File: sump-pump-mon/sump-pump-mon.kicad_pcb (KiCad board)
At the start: 2 copper layers, 111.8 x 61 mm, 37 parts, among them J1 Main Input, J2 Wall Power, J3 Battery, J4 Display_Conn, J5 Aux Input, J6 I2C, SW3 MODE, SW4 POWER, U1 L7805, U2 4N25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

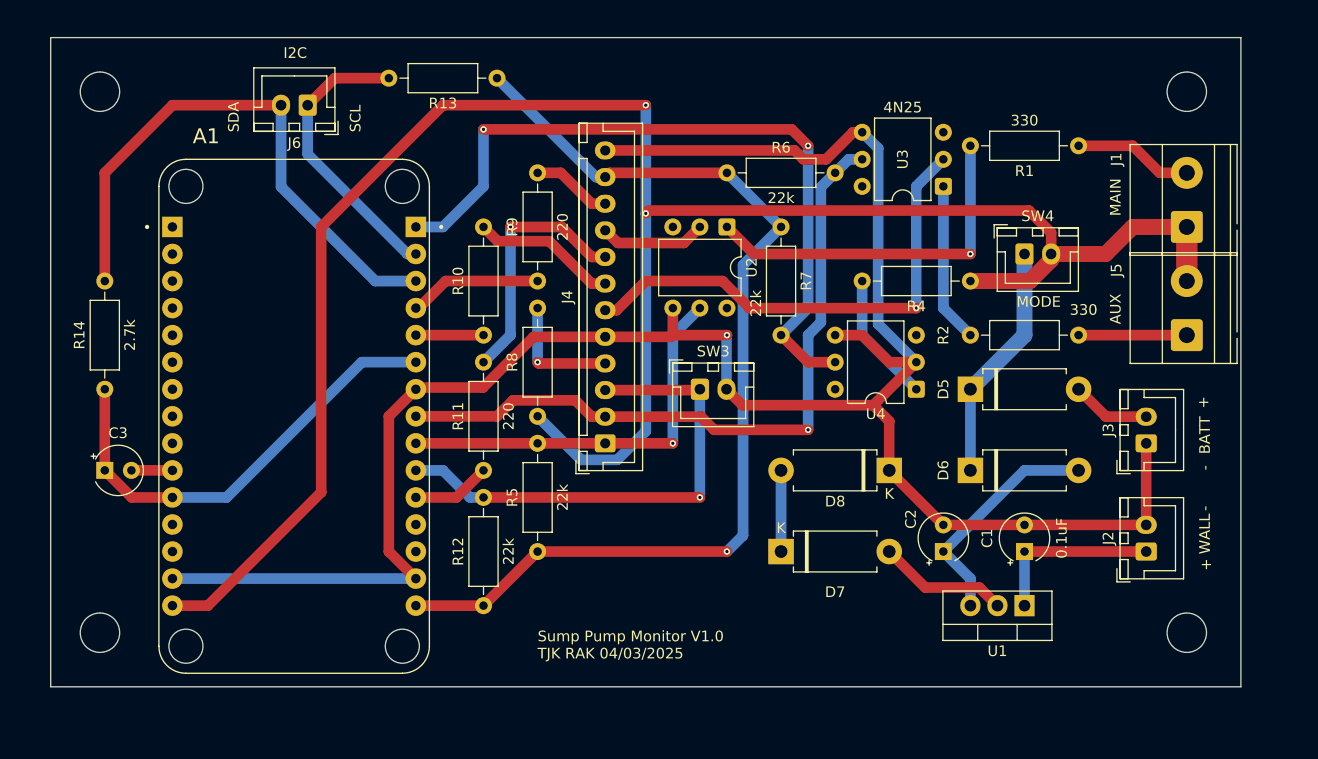
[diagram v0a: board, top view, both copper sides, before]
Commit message: Redid layout to shrink size and add ground plane
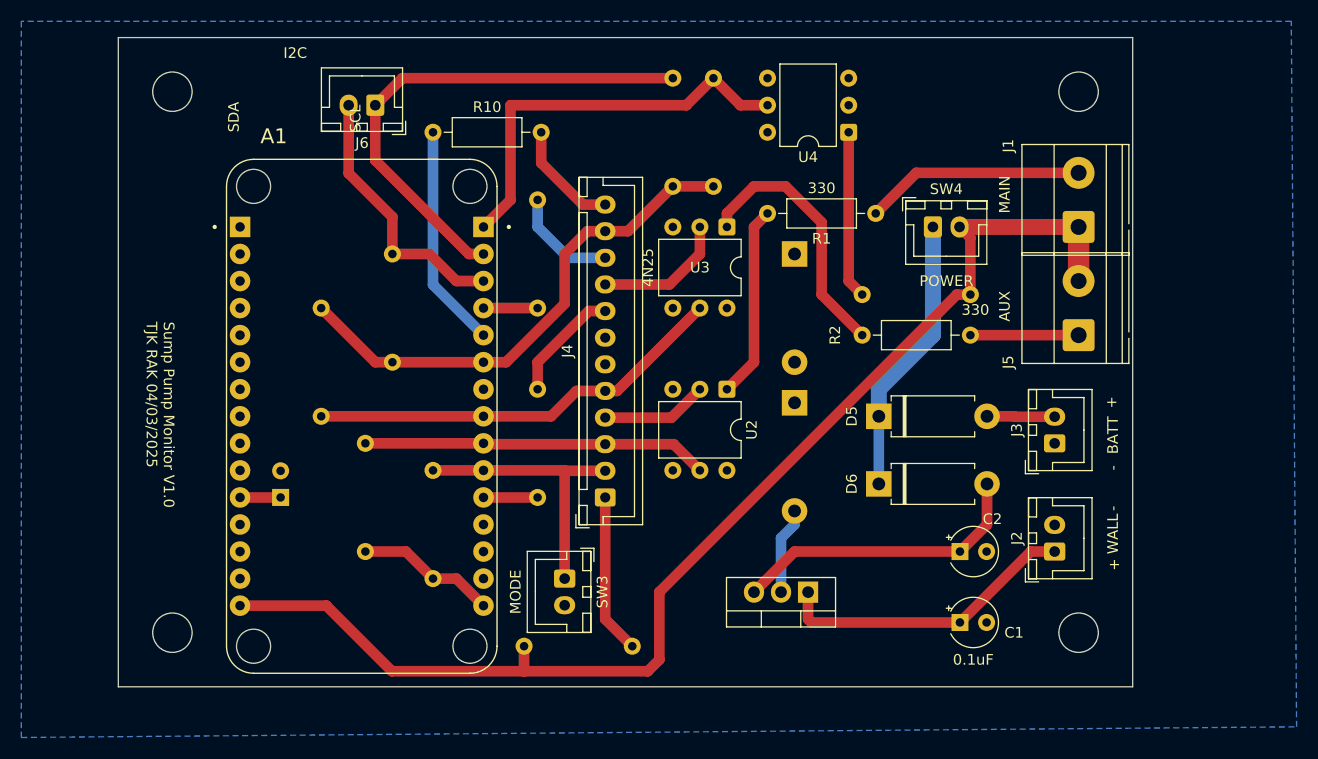
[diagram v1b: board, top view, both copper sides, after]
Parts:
- C3, D7, D8, R11, R12, R13, R14, R4, R5, R6, R7, R8, R9: moved to B.Cu
- moved R6 40.2 mm to (137.2, 43.2), turned to -90 degrees
- moved R14 27.1 mm to (143.8, 48.3)
- moved U4 25.0 mm to (186.7, 26.7)
- moved D8 22.2 mm to (181.6, 38.1), turned to -90 degrees
- moved SW3 21.8 mm to (160.0, 68.6), turned to -90 degrees
- moved R8 21.6 mm to (156.2, 74.9), turned to 0 degrees
- moved U3 20.7 mm to (175.3, 35.6), turned to -90 degrees
- moved U1 20.4 mm to (182.9, 69.8)
- moved R1 20.1 mm to (189.2, 34.3)
- moved R10 19.6 mm to (147.7, 26.7), turned to 0 degrees
- moved R13 19.4 mm to (170.2, 31.8), turned to 90 degrees
- moved C3 16.7 mm to (133.3, 61.0), turned to 90 degrees
- moved R5 16.2 mm to (141.3, 66.0)
- moved U2 15.2 mm to (175.3, 50.8)
- moved D7 14.0 mm to (181.6, 52.1), turned to -90 degrees
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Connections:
- J4 pad 1: Main_Input -> LED_6V
- J4 pad 12: GND -> LED_YELLOW
- J4 pad 2: Aux_Input -> Mode
- J4 pad 3: Mode -> Main_Input
- J4 pad 4: LED_6V -> LED_MAIN
- J4 pad 5: GND -> Aux_Input
- J4 pad 6: LED_AUX -> GND
- J4 pad 7: LED_YELLOW -> GND
- J4 pad 9: LED_MAIN -> LED_AUX
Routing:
- net GND: track 204.2 -> 0.00 mm, vias 1 -> 0
- net Vin: track 191.0 -> 114.9 mm, vias 2 -> 0
- net +3.3V: track 139.8 -> 65.5 mm, vias 1 -> 0
- net LED_AUX: track 46.4 -> 12.6 mm, vias 1 -> 0
- net Power_Failure: track 69.4 -> 38.7 mm, vias 2 -> 0
- net Net-(A1B-D2): track 53.3 -> 25.3 mm
- net Aux_Input: track 66.8 -> 39.9 mm, vias 1 -> 0
- net Net-(A1B-D1): track 27.3 -> 48.0 mm
- net Mode: track 46.8 -> 26.3 mm, vias 1 -> 0
- net Net-(R1-Pad2): track 34.1 -> 18.1 mm, vias 1 -> 0
- net Net-(A1B-D4): track 6.35 -> 21.0 mm
- net LED_BLUE: track 23.8 -> 10.9 mm, vias 1 -> 0
- net Net-(J2-Pin_1): track 16.5 -> 28.6 mm
- net Net-(R2-Pad2): track 15.0 -> 24.8 mm
- net Net-(J1-Pin_2): track 11.2 -> 20.6 mm
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- added copper zone on B.Cu, net GND
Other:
- board size 111.8 x 61 mm -> 95.3 x 61 mm
- board text removed: "MODE"

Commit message: Shrink layout a bit more
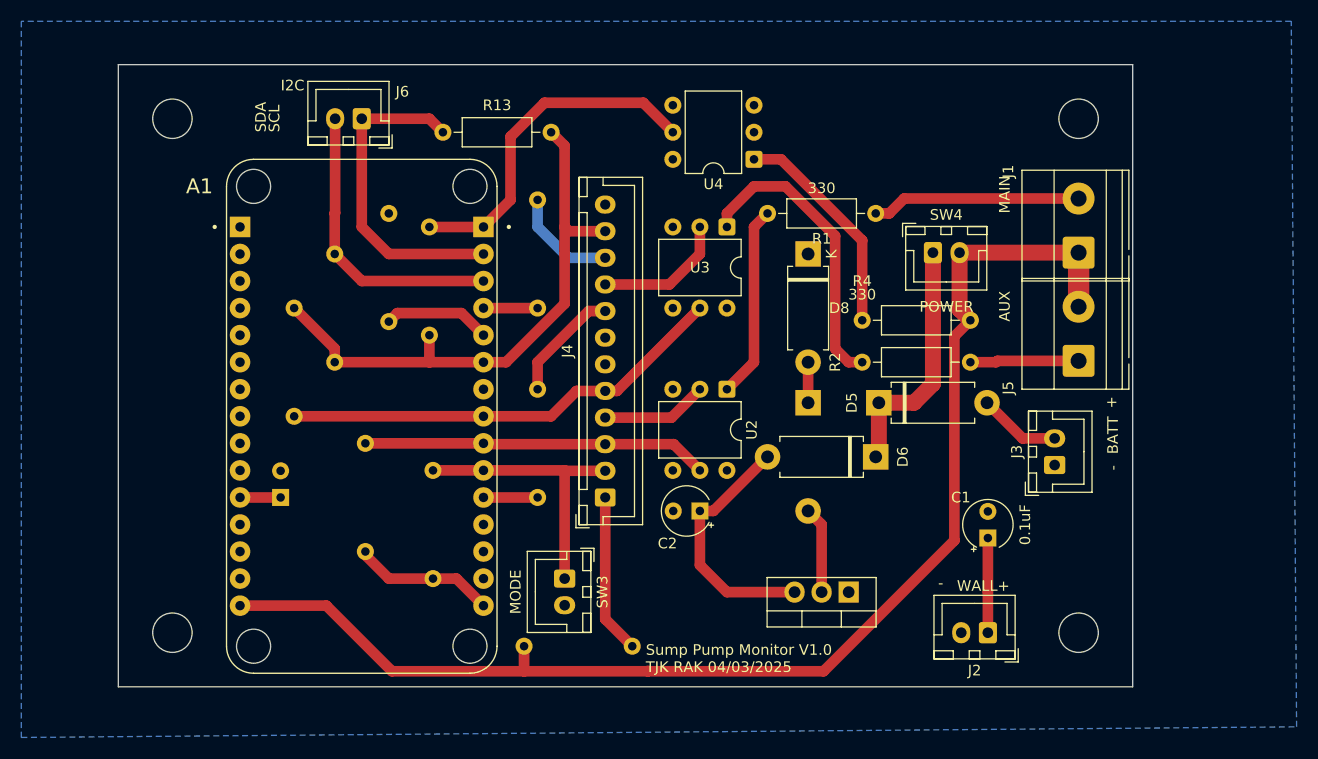
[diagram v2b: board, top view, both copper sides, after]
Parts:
- D8, R13, R4: moved to F.Cu
- R10: moved to B.Cu
- moved R7 30.1 mm to (147.3, 45.7)
- moved C2 24.7 mm to (172.7, 62.2), turned to 180 degrees
- moved R10 18.3 mm to (143.5, 44.5), turned to 90 degrees
- moved R13 12.5 mm to (158.8, 26.7), turned to 180 degrees
- moved J2 9.87 mm to (199.8, 73.7), turned to 180 degrees
- moved U4 9.25 mm to (177.8, 29.2)
- moved C1 8.35 mm to (199.8, 64.8), turned to 90 degrees
- moved R14 5.42 mm to (138.4, 48.3)
- moved U1 3.81 mm to (186.7, 69.8)
- moved D6 2.56 mm to (189.2, 57.1), turned to 180 degrees
- moved H1 2.54 mm to (208.3, 25.4)
- moved H3 2.54 mm to (123.2, 25.4)
- moved R2 2.54 mm to (198.1, 48.3)
- moved R6 2.54 mm to (134.6, 43.2)
- moved J1 2.41 mm to (208.3, 38.0)
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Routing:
- net Net-(J2-Pin_1): track 28.6 -> 8.89 mm
- net Net-(A1B-D1): track 48.0 -> 30.8 mm
- net Net-(A1B-D4): track 21.0 -> 10.1 mm
- net LED_YELLOW: track 10.5 -> 0.00 mm
- net Vin: track 114.9 -> 121.5 mm
- net Power_Failure: track 38.7 -> 32.3 mm
- net +3.3V: track 65.5 -> 70.9 mm
- net Net-(R4-Pad2): track 15.8 -> 20.8 mm
- net Net-(D6-A): track 28.3 -> 23.5 mm
- net Net-(D7-K): track 0.00 -> 3.81 mm
- net Net-(R2-Pad2): track 24.8 -> 28.1 mm
- net Net-(D5-K): track 26.2 -> 23.3 mm
- net Aux_Input: track 39.9 -> 42.4 mm
- net Net-(A1B-D2): track 25.3 -> 27.7 mm
- net Net-(D5-A): track 6.37 -> 7.74 mm
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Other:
- board size 95.3 x 61 mm -> 95.3 x 58.4 mm

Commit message: Layout polishing
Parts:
- moved J2 10.7 mm to (205.7, 64.8), turned to 0 degrees
- moved C1 7.45 mm to (194.3, 59.7)
- moved J3 2.37 mm to (208.3, 57.1), turned to 180 degrees
- moved U1 1.91 mm to (186.7, 71.8)
- moved R13 1.27 mm to (160.0, 26.7)
- moved D8 1.27 mm to (181.6, 38.1)
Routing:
- net Net-(J2-Pin_1): track 8.89 -> 28.8 mm
- net Net-(D5-A): track 7.74 -> 10.6 mm
- net Net-(D7-A): track 8.15 -> 10.1 mm
- net Net-(A1B-D1): track 30.8 -> 32.1 mm
- net Aux_Input: track 42.4 -> 43.5 mm
- net Net-(D6-A): track 23.5 -> 24.3 mm
- net Net-(D7-K): track 3.81 -> 4.34 mm

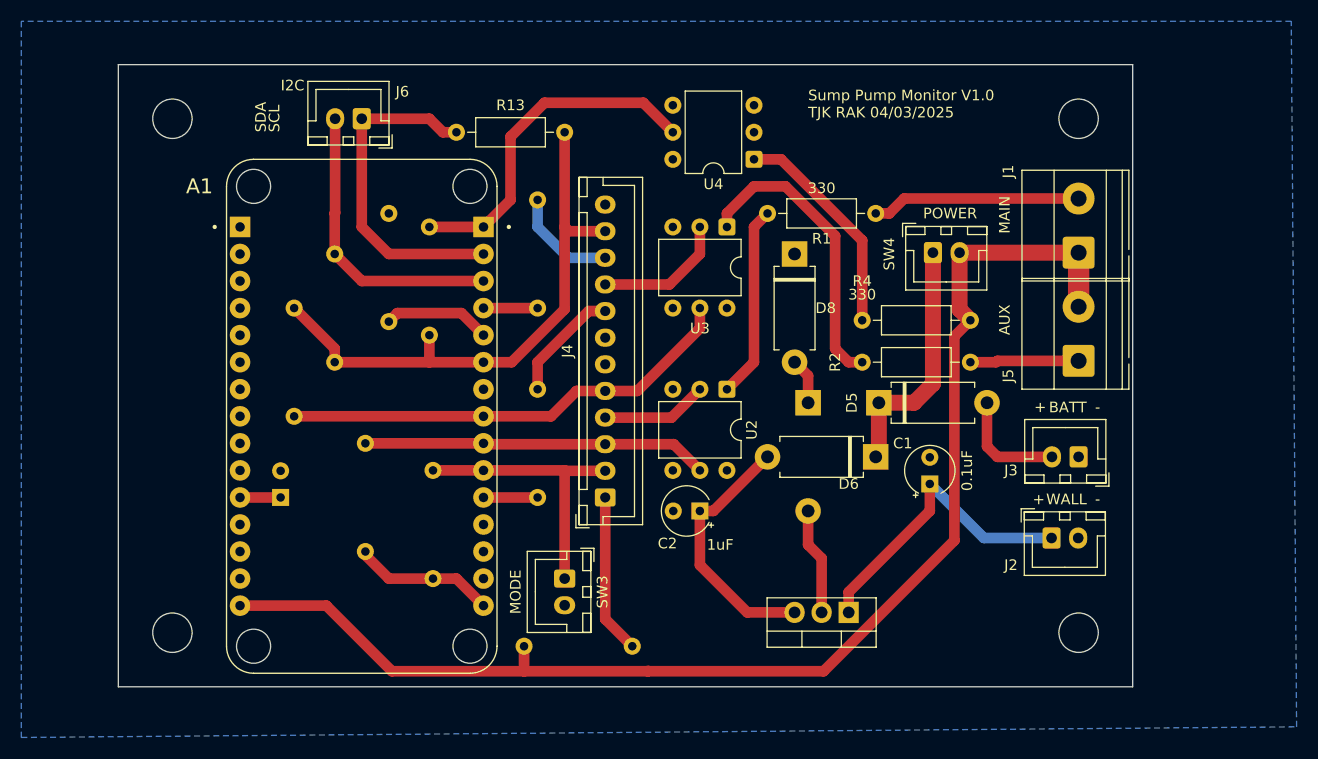
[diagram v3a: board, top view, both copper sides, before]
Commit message: Fix missing connection, move C1 to top, shift J2 down
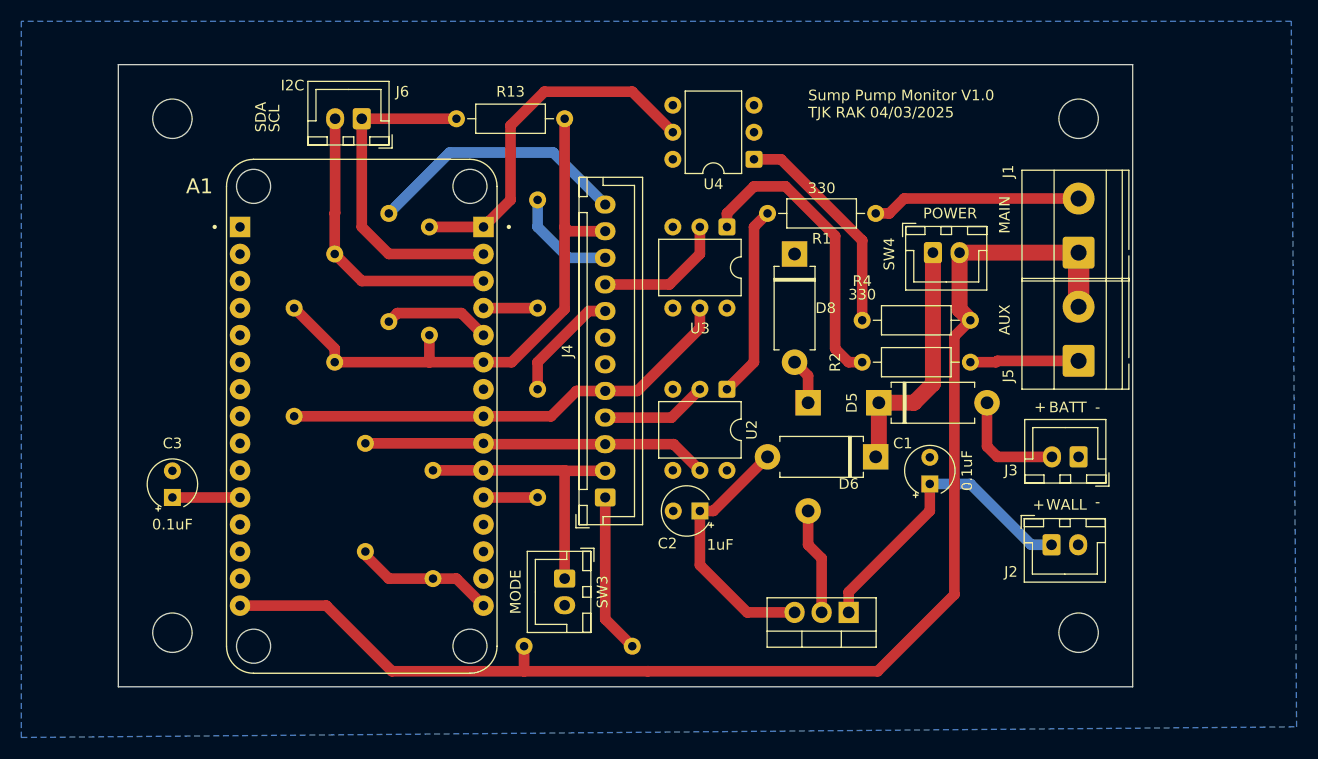
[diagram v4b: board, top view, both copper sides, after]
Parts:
- C3: moved to F.Cu
- moved C3 10.2 mm to (123.2, 61.0)
- moved R13 1.27 mm to (160.0, 25.4)
- moved J2 0.64 mm to (205.7, 65.4)
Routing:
- net LED_YELLOW: track 0.00 -> 24.7 mm
- net +3.3V: track 70.6 -> 74.5 mm
- net Vin: track 121.5 -> 124.4 mm
- net Power_Failure: track 32.3 -> 33.8 mm
- net Net-(A1B-D1): track 32.1 -> 31.5 mm

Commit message: Add GND to I2C connector
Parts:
- J6: footprint Connector_JST:JST_XH_B2B-XH-A_1x02_P2.50mm_Vertical -> Connector_JST:JST_XH_B3B-XH-A_1x03_P2.50mm_Vertical
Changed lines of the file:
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@@
 		)
 	)
-	(footprint "Connector_JST:JST_XH_B2B-XH-A_1x02_P2.50mm_Vertical"
+	(footprint "Connector_JST:JST_XH_B3B-XH-A_1x03_P2.50mm_Vertical"
 		(layer "F.Cu")
 		(at 140.97 25.4 180)
-		(descr "JST XH series connector, B2B-XH-A (http://www.jst-mfg.com/product/pdf/eng/eXH.pdf), generated with kicad-footprint-generator")
+		(descr "JST XH series connector, B3B-XH-A (http://www.jst-mfg.com/product/pdf/eng/eXH.pdf), generated with kicad-footprint-generator")
 		(tags "connector JST XH vertical")
 		(property "Reference" "J6"
-			(at -3.81 2.54 0)
+			(at 2.5 -3.55 180)
 			(layer "F.SilkS")
 			(effects
@@
 		)
 		(property "Value" "I2C"
-			(at 1.25 4.6 0)
+			(at 2.5 4.6 180)
 			(layer "F.Fab")
 			(effects
@@
 		)
 		(property "Datasheet" ""
-			(at 0 0 0)
+			(at 0 0 180)
 			(layer "F.Fab")
 			(hide yes)
@@
 			)
 		)
-		(property "Description" "Generic connector, single row, 01x02, script generated"
-			(at 0 0 0)
+		(property "Description" "Generic connector, single row, 01x03, script generated"
+			(at 0 0 180)
 			(layer "F.Fab")
 			(hide yes)
@@
 		(attr through_hole)
 		(fp_line
-			(start 5.06 3.51)
-			(end 5.06 -2.46)
+			(start 7.56 3.51)
+			(end 7.56 -2.46)
 			(stroke
 				(width 0.12)
@@
 		)
 		(fp_line
-			(start 5.06 -2.46)
+			(start 7.56 -2.46)
 			(end -2.56 -2.46)
 			(stroke
@@
 		)
 		(fp_line
-			(start 5.05 -0.2)
-			(end 4.3 -0.2)
+			(start 7.55 -0.2)
+			(end 6.8 -0.2)
 			(stroke
 				(width 0.12)
@@
 		)
 		(fp_line
-			(start 5.05 -1.7)
-			(end 5.05 -2.45)
+			(start 7.55 -1.7)
+			(end 7.55 -2.45)
 			(stroke
 				(width 0.12)
@@
 		)
 		(fp_line
-			(start 5.05 -2.45)
-			(end 3.25 -2.45)
+			(start 7.55 -2.45)
+			(end 5.75 -2.45)
 			(stroke
 				(width 0.12)
@@
 		)
 		(fp_line
-			(start 4.3 2.75)
-			(end 1.25 2.75)
+			(start 6.8 2.75)
+			(end 2.5 2.75)
 			(stroke
 				(width 0.12)
@@
 		)
 		(fp_line
-			(start 4.3 -0.2)
-			(end 4.3 2.75)
+			(start 6.8 -0.2)
+			(end 6.8 2.75)
 			(stroke
 				(width 0.12)
@@
 		)
 		(fp_line
-			(start 3.25 -1.7)
-			(end 5.05 -1.7)
+			(start 5.75 -1.7)
+			(end 7.55 -1.7)
 			(stroke
 				(width 0.12)
@@
 		)
 		(fp_line
-			(start 3.25 -2.45)
-			(end 3.25 -1.7)
+			(start 5.75 -2.45)
+			(end 5.75 -1.7)
 			(stroke
 				(width 0.12)
@@
 		)
 		(fp_line
-			(start 1.75 -1.7)
-			(end 1.75 -2.45)
+			(start 4.25 -1.7)
+			(end 4.25 -2.45)
 			(stroke
 				(width 0.12)
@@
 		)
 		(fp_line
-			(start 1.75 -2.45)
+			(start 4.25 -2.45)
 			(end 0.75 -2.45)
 			(stroke
@@
 		(fp_line
 			(start 0.75 -1.7)
-			(end 1.75 -1.7)
+			(end 4.25 -1.7)
 			(stroke
 				(width 0.12)
@@
 		(fp_line
 			(start -1.8 2.75)
-			(end 1.25 2.75)
+			(end 2.5 2.75)
 			(stroke
 				(width 0.12)
@@
 		(fp_line
 			(start -2.56 3.51)
-			(end 5.06 3.51)
+			(end 7.56 3.51)
 			(stroke
 				(width 0.12)
@@
 		)
 		(fp_line
-			(start 5.45 3.9)
-			(end 5.45 -2.85)
+			(start 7.95 3.9)
+			(end 7.95 -2.85)
 			(stroke
 				(width 0.05)
@@
 		)
 		(fp_line
-			(start 5.45 -2.85)
+			(start 7.95 -2.85)
 			(end -2.95 -2.85)
 			(stroke
@@
 		(fp_line
 			(start -2.95 3.9)
-			(end 5.45 3.9)
+			(end 7.95 3.9)
 			(stroke
 				(width 0.05)
@@
 		)
 		(fp_line
-			(start 4.95 3.4)
-			(end 4.95 -2.35)
+			(start 7.45 3.4)
+			(end 7.45 -2.35)
 			(stroke
 				(width 0.1)
@@
 		)
 		(fp_line
-			(start 4.95 -2.35)
+			(start 7.45 -2.35)
 			(end -2.45 -2.35)
 			(stroke
@@
 		(fp_line
 			(start -2.45 3.4)
-			(end 4.95 3.4)
+			(end 7.45 3.4)
 			(stroke
 				(width 0.1)
@@
 		)
 		(fp_text user "${REFERENCE}"
-			(at 1.25 2.7 0)
+			(at 2.5 2.7 180)
 			(layer "F.Fab")
 			(effects
@@
 		(pad "1" thru_hole roundrect
 			(at 0 0 180)
-			(size 1.7 2)
-			(drill 1)
+			(size 1.7 1.95)
+			(drill 0.95)
 			(layers "*.Cu" "*.Mask")
 			(remove_unused_layers no)
@@
 		(pad "2" thru_hole oval
 			(at 2.5 0 180)
-			(size 1.7 2)
-			(drill 1)
+			(size 1.7 1.95)
+			(drill 0.95)
 			(layers "*.Cu" "*.Mask")
 			(remove_unused_layers no)
@@
 			(pintype "passive")
 		)
+		(pad "3" thru_hole oval
+			(at 5 0 180)
+			(size 1.7 1.95)
+			(drill 0.95)
+			(layers "*.Cu" "*.Mask")
+			(remove_unused_layers no)
+			(net 20 "GND")
+			(pinfunction "Pin_3")
+			(pintype "passive")
+		)
 		(embedded_fonts no)
-		(model "${KICAD9_3DMODEL_DIR}/Connector_JST.3dshapes/JST_XH_B2B-XH-A_1x02_P2.50mm_Vertical.wrl"
+		(model "${KICAD9_3DMODEL_DIR}/Connector_JST.3dshapes/JST_XH_B3B-XH-A_1x03_P2.50mm_Vertical.wrl"
 			(offset
 				(xyz 0 0 0)
@@
 	)
 	(gr_text "SDA"
-		(at 132.08 26.67 90)
+		(at 129.54 27.305 90)
 		(layer "F.SilkS")
 		(effects
@@
 	)
 	(gr_text "SCL"
-		(at 133.35 26.67 90)
+		(at 130.81 27.305 90)
 		(layer "F.SilkS")
 		(effects
@@
 	)
 	(gr_text "I2C"
-		(at 133.35 22.86 0)
+		(at 130.175 22.86 0)
 		(layer "F.SilkS")
 		(effects
